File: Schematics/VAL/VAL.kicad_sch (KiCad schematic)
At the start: 2 parts

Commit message: Fox NOVRAM address bus
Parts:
- U101, U102: value (none) -> ~
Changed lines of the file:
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@@
   (wire (pts (xy 566.42 241.3) (xy 566.42 243.84) ) (stroke (width 0) (type default) ) )
   (wire (pts (xy 566.42 259.08) (xy 566.42 261.62) ) (stroke (width 0) (type default) ) )
-  (symbol (lib_id "r1000:PU") (at 566.42 241.3 0) (unit 1) (in_bom yes) (on_board yes) (property "Reference" "#PWR0102" (id 0) (at 566.42 241.3 0) (effects (font (size 1.27 1.27) ) hide ) ) (property "Value" "" (id 1) (at 566.42 241.3 0) (effects (font (size 1.27 1.27) ) hide ) ) (property "Footprint" "" (id 2) (at 566.42 241.3 0) (effects (font (size 1.27 1.27) ) hide ) ) (property "Datasheet" "" (id 3) (at 566.42 241.3 0) (effects (font (size 1.27 1.27) ) hide ) ) (pin "1" ) )
-  (symbol (lib_id "r1000:Pull_Down") (at 566.42 259.08 0) (unit 1) (in_bom yes) (on_board yes) (property "Reference" "U102" (id 0) (at 566.42 259.08 0) (effects (font (size 1.27 1.27) ) ) ) (property "Value" "" (id 1) (at 566.42 255.27 0) (effects (font (size 2.54 2.54) ) ) ) (property "Footprint" "" (id 2) (at 566.42 259.08 0) (effects (font (size 1.27 1.27) ) hide ) ) (property "Datasheet" "" (id 3) (at 566.42 259.08 0) (effects (font (size 1.27 1.27) ) hide ) ) (pin "1" ) )
-  (symbol (lib_id "r1000:Pull_Up") (at 566.42 243.84 0) (unit 1) (in_bom yes) (on_board yes) (property "Reference" "U101" (id 0) (at 566.42 243.84 0) (effects (font (size 1.27 1.27) ) ) ) (property "Value" "" (id 1) (at 566.42 247.65 0) (effects (font (size 2.54 2.54) ) ) ) (property "Footprint" "" (id 2) (at 566.42 243.84 0) (effects (font (size 1.27 1.27) ) hide ) ) (property "Datasheet" "" (id 3) (at 566.42 243.84 0) (effects (font (size 1.27 1.27) ) hide ) ) (pin "1" ) )
-  (symbol (lib_id "r1000:PD") (at 566.42 261.62 0) (unit 1) (in_bom no) (on_board yes) (property "Reference" "#PWR0101" (id 0) (at 566.42 261.62 0) (effects (font (size 1.27 1.27) ) hide ) ) (property "Value" "" (id 1) (at 566.42 261.62 0) (effects (font (size 1.27 1.27) ) hide ) ) (property "Footprint" "" (id 2) (at 566.42 261.62 0) (effects (font (size 1.27 1.27) ) hide ) ) (property "Datasheet" "" (id 3) (at 566.42 261.62 0) (effects (font (size 1.27 1.27) ) hide ) ) (pin "1" ) )
+  (symbol (lib_id "r1000:PU") (at 566.42 241.3 0) (unit 1) (in_bom yes) (on_board yes) (property "Reference" "#PWR0102" (id 0) (at 566.42 241.3 0) (effects (font (size 1.27 1.27) ) hide ) ) (property "Value" "~" (id 1) (at 566.42 241.3 0) (effects (font (size 1.27 1.27) ) hide ) ) (property "Footprint" "" (id 2) (at 566.42 241.3 0) (effects (font (size 1.27 1.27) ) hide ) ) (property "Datasheet" "" (id 3) (at 566.42 241.3 0) (effects (font (size 1.27 1.27) ) hide ) ) (pin "1" ) )
+  (symbol (lib_id "r1000:Pull_Down") (at 566.42 259.08 0) (unit 1) (in_bom yes) (on_board yes) (property "Reference" "U102" (id 0) (at 566.42 259.08 0) (effects (font (size 1.27 1.27) ) ) ) (property "Value" "~" (id 1) (at 566.42 255.27 0) (effects (font (size 2.54 2.54) ) ) ) (property "Footprint" "" (id 2) (at 566.42 259.08 0) (effects (font (size 1.27 1.27) ) hide ) ) (property "Datasheet" "" (id 3) (at 566.42 259.08 0) (effects (font (size 1.27 1.27) ) hide ) ) (pin "1" ) )
+  (symbol (lib_id "r1000:Pull_Up") (at 566.42 243.84 0) (unit 1) (in_bom yes) (on_board yes) (property "Reference" "U101" (id 0) (at 566.42 243.84 0) (effects (font (size 1.27 1.27) ) ) ) (property "Value" "~" (id 1) (at 566.42 247.65 0) (effects (font (size 2.54 2.54) ) ) ) (property "Footprint" "" (id 2) (at 566.42 243.84 0) (effects (font (size 1.27 1.27) ) hide ) ) (property "Datasheet" "" (id 3) (at 566.42 243.84 0) (effects (font (size 1.27 1.27) ) hide ) ) (pin "1" ) )
+  (symbol (lib_id "r1000:PD") (at 566.42 261.62 0) (unit 1) (in_bom no) (on_board yes) (property "Reference" "#PWR0101" (id 0) (at 566.42 261.62 0) (effects (font (size 1.27 1.27) ) hide ) ) (property "Value" "~" (id 1) (at 566.42 261.62 0) (effects (font (size 1.27 1.27) ) hide ) ) (property "Footprint" "" (id 2) (at 566.42 261.62 0) (effects (font (size 1.27 1.27) ) hide ) ) (property "Datasheet" "" (id 3) (at 566.42 261.62 0) (effects (font (size 1.27 1.27) ) hide ) ) (pin "1" ) )
   (text "Board: VAL Branch: megacomp2" (at 7.62 370.84 0) (effects (font (size 7.62 7.62) (thickness 1.27) bold ) (justify left bottom) ) )
   (sheet_instances

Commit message: Megacom WCS + parity
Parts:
- U101, U102: value ~ -> (none)
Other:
- note added: "WRITABLE CONTROL STORE - WCS BITS 32 TO 38 AND PARITY <6>"
- note removed: "WRITABLE CONTROL STORE - WCS BITS 32 TO 38 AND PARITY"
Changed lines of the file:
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@@
   (wire (pts (xy 566.42 241.3) (xy 566.42 243.84) ) (stroke (width 0) (type default) ) )
   (wire (pts (xy 566.42 259.08) (xy 566.42 261.62) ) (stroke (width 0) (type default) ) )
-  (symbol (lib_id "r1000:PU") (at 566.42 241.3 0) (unit 1) (in_bom yes) (on_board yes) (property "Reference" "#PWR0102" (id 0) (at 566.42 241.3 0) (effects (font (size 1.27 1.27) ) hide ) ) (property "Value" "~" (id 1) (at 566.42 241.3 0) (effects (font (size 1.27 1.27) ) hide ) ) (property "Footprint" "" (id 2) (at 566.42 241.3 0) (effects (font (size 1.27 1.27) ) hide ) ) (property "Datasheet" "" (id 3) (at 566.42 241.3 0) (effects (font (size 1.27 1.27) ) hide ) ) (pin "1" ) )
-  (symbol (lib_id "r1000:Pull_Down") (at 566.42 259.08 0) (unit 1) (in_bom yes) (on_board yes) (property "Reference" "U102" (id 0) (at 566.42 259.08 0) (effects (font (size 1.27 1.27) ) ) ) (property "Value" "~" (id 1) (at 566.42 255.27 0) (effects (font (size 2.54 2.54) ) ) ) (property "Footprint" "" (id 2) (at 566.42 259.08 0) (effects (font (size 1.27 1.27) ) hide ) ) (property "Datasheet" "" (id 3) (at 566.42 259.08 0) (effects (font (size 1.27 1.27) ) hide ) ) (pin "1" ) )
-  (symbol (lib_id "r1000:Pull_Up") (at 566.42 243.84 0) (unit 1) (in_bom yes) (on_board yes) (property "Reference" "U101" (id 0) (at 566.42 243.84 0) (effects (font (size 1.27 1.27) ) ) ) (property "Value" "~" (id 1) (at 566.42 247.65 0) (effects (font (size 2.54 2.54) ) ) ) (property "Footprint" "" (id 2) (at 566.42 243.84 0) (effects (font (size 1.27 1.27) ) hide ) ) (property "Datasheet" "" (id 3) (at 566.42 243.84 0) (effects (font (size 1.27 1.27) ) hide ) ) (pin "1" ) )
-  (symbol (lib_id "r1000:PD") (at 566.42 261.62 0) (unit 1) (in_bom no) (on_board yes) (property "Reference" "#PWR0101" (id 0) (at 566.42 261.62 0) (effects (font (size 1.27 1.27) ) hide ) ) (property "Value" "~" (id 1) (at 566.42 261.62 0) (effects (font (size 1.27 1.27) ) hide ) ) (property "Footprint" "" (id 2) (at 566.42 261.62 0) (effects (font (size 1.27 1.27) ) hide ) ) (property "Datasheet" "" (id 3) (at 566.42 261.62 0) (effects (font (size 1.27 1.27) ) hide ) ) (pin "1" ) )
+  (symbol (lib_id "r1000:PU") (at 566.42 241.3 0) (unit 1) (in_bom yes) (on_board yes) (property "Reference" "#PWR0102" (id 0) (at 566.42 241.3 0) (effects (font (size 1.27 1.27) ) hide ) ) (property "Value" "" (id 1) (at 566.42 241.3 0) (effects (font (size 1.27 1.27) ) hide ) ) (property "Footprint" "" (id 2) (at 566.42 241.3 0) (effects (font (size 1.27 1.27) ) hide ) ) (property "Datasheet" "" (id 3) (at 566.42 241.3 0) (effects (font (size 1.27 1.27) ) hide ) ) (pin "1" ) )
+  (symbol (lib_id "r1000:Pull_Down") (at 566.42 259.08 0) (unit 1) (in_bom yes) (on_board yes) (property "Reference" "U102" (id 0) (at 566.42 259.08 0) (effects (font (size 1.27 1.27) ) ) ) (property "Value" "" (id 1) (at 566.42 255.27 0) (effects (font (size 2.54 2.54) ) ) ) (property "Footprint" "" (id 2) (at 566.42 259.08 0) (effects (font (size 1.27 1.27) ) hide ) ) (property "Datasheet" "" (id 3) (at 566.42 259.08 0) (effects (font (size 1.27 1.27) ) hide ) ) (pin "1" ) )
+  (symbol (lib_id "r1000:Pull_Up") (at 566.42 243.84 0) (unit 1) (in_bom yes) (on_board yes) (property "Reference" "U101" (id 0) (at 566.42 243.84 0) (effects (font (size 1.27 1.27) ) ) ) (property "Value" "" (id 1) (at 566.42 247.65 0) (effects (font (size 2.54 2.54) ) ) ) (property "Footprint" "" (id 2) (at 566.42 243.84 0) (effects (font (size 1.27 1.27) ) hide ) ) (property "Datasheet" "" (id 3) (at 566.42 243.84 0) (effects (font (size 1.27 1.27) ) hide ) ) (pin "1" ) )
+  (symbol (lib_id "r1000:PD") (at 566.42 261.62 0) (unit 1) (in_bom no) (on_board yes) (property "Reference" "#PWR0101" (id 0) (at 566.42 261.62 0) (effects (font (size 1.27 1.27) ) hide ) ) (property "Value" "" (id 1) (at 566.42 261.62 0) (effects (font (size 1.27 1.27) ) hide ) ) (property "Footprint" "" (id 2) (at 566.42 261.62 0) (effects (font (size 1.27 1.27) ) hide ) ) (property "Datasheet" "" (id 3) (at 566.42 261.62 0) (effects (font (size 1.27 1.27) ) hide ) ) (pin "1" ) )
   (text "Board: VAL Branch: megacomp2" (at 7.62 370.84 0) (effects (font (size 7.62 7.62) (thickness 1.27) bold ) (justify left bottom) ) )
   (sheet_instances
@@
   (sheet (at 266.70 88.90) (size 20.32 5.08) (property "Sheet name" "Page 55" (id 0) (at 289.56 93.98 0) (effects (font (size 2.54 2.54) ) (justify left bottom) ) ) (property "Sheet file" "pg_55.kicad_sch" (id 1) (at 289.56 91.44 0) (effects (justify left bottom) hide ) ) (fill (color 192 192 192 1.0) ) )
   (text "WRITABLE CONTROL STORE - WCS BITS 16 to 31 <6>" (at 307.34 93.98 0) (effects (font (size 2.54 2.54) ) (justify left bottom) ) )
-  (sheet (at 266.70 96.52) (size 20.32 5.08) (property "Sheet name" "Page 56" (id 0) (at 289.56 101.60 0) (effects (font (size 2.54 2.54) ) (justify left bottom) ) ) (property "Sheet file" "pg_56.kicad_sch" (id 1) (at 289.56 99.06 0) (effects (justify left bottom) hide ) ) )
-  (text "WRITABLE CONTROL STORE - WCS BITS 32 TO 38 AND PARITY" (at 307.34 101.60 0) (effects (font (size 2.54 2.54) ) (justify left bottom) ) )
+  (sheet (at 266.70 96.52) (size 20.32 5.08) (property "Sheet name" "Page 56" (id 0) (at 289.56 101.60 0) (effects (font (size 2.54 2.54) ) (justify left bottom) ) ) (property "Sheet file" "pg_56.kicad_sch" (id 1) (at 289.56 99.06 0) (effects (justify left bottom) hide ) ) (fill (color 192 192 192 1.0) ) )
+  (text "WRITABLE CONTROL STORE - WCS BITS 32 TO 38 AND PARITY <6>" (at 307.34 101.60 0) (effects (font (size 2.54 2.54) ) (justify left bottom) ) )
   (sheet (at 266.70 104.14) (size 20.32 5.08) (property "Sheet name" "Page 57" (id 0) (at 289.56 109.22 0) (effects (font (size 2.54 2.54) ) (justify left bottom) ) ) (property "Sheet file" "pg_57.kicad_sch" (id 1) (at 289.56 106.68 0) (effects (justify left bottom) hide ) ) )
   (text "WRITABLE CONTROL STORE - MICRO INSTRUCTION REGISTER" (at 307.34 109.22 0) (effects (font (size 2.54 2.54) ) (justify left bottom) ) )

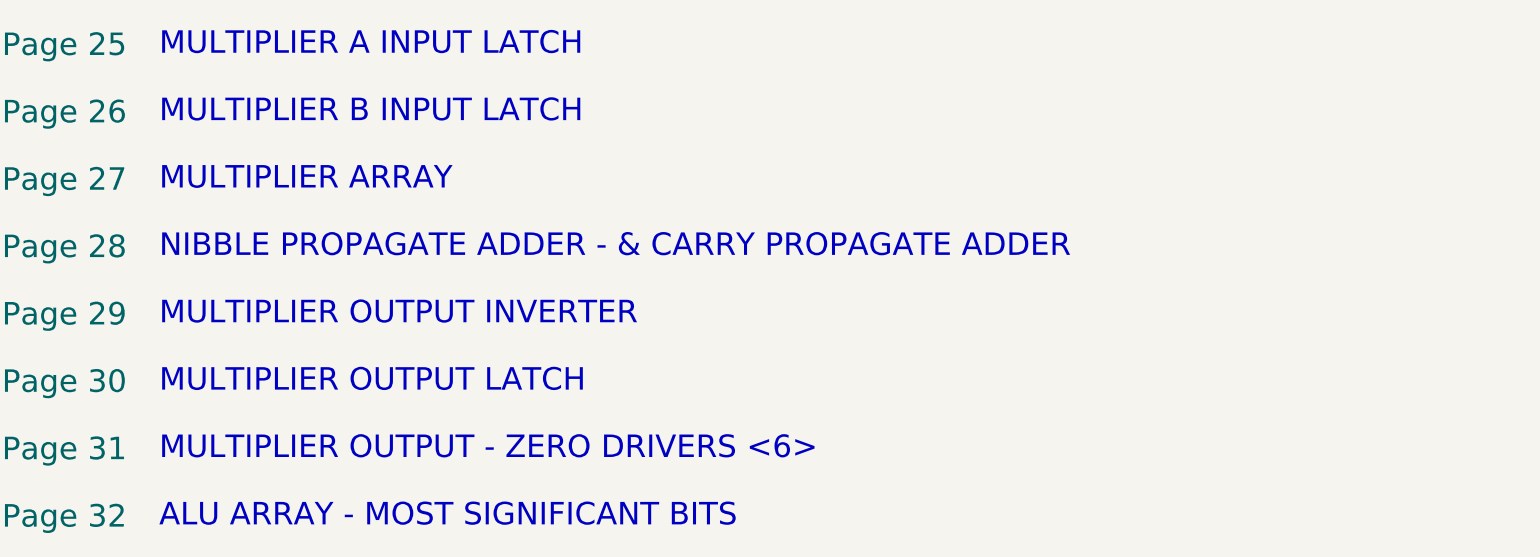
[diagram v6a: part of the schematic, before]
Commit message: Megacomp/polish work on VAL (incl. megacomp multiplier)
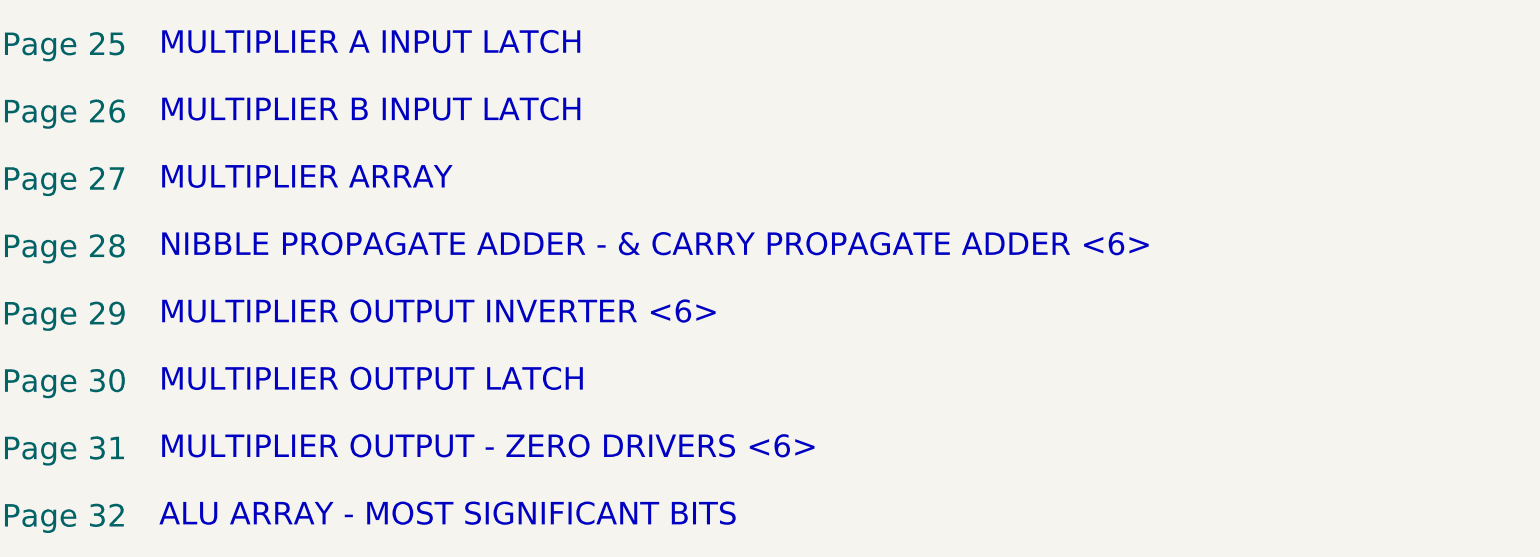
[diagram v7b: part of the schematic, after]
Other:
- note added: "MULTIPLIER OUTPUT INVERTER <6>"
- note added: "NIBBLE PROPAGATE ADDER - & CARRY PROPAGATE ADDER <6>"
- note removed: "MULTIPLIER OUTPUT INVERTER"
- note removed: "NIBBLE PROPAGATE ADDER - & CARRY PROPAGATE ADDER"
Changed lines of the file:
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@@
   (sheet (at 12.70 218.44) (size 20.32 5.08) (property "Sheet name" "Page 27" (id 0) (at 35.56 223.52 0) (effects (font (size 2.54 2.54) ) (justify left bottom) ) ) (property "Sheet file" "pg_27.kicad_sch" (id 1) (at 35.56 220.98 0) (effects (justify left bottom) hide ) ) )
   (text "MULTIPLIER ARRAY" (at 53.34 223.52 0) (effects (font (size 2.54 2.54) ) (justify left bottom) ) )
-  (sheet (at 12.70 226.06) (size 20.32 5.08) (property "Sheet name" "Page 28" (id 0) (at 35.56 231.14 0) (effects (font (size 2.54 2.54) ) (justify left bottom) ) ) (property "Sheet file" "pg_28.kicad_sch" (id 1) (at 35.56 228.60 0) (effects (justify left bottom) hide ) ) )
-  (text "NIBBLE PROPAGATE ADDER - & CARRY PROPAGATE ADDER" (at 53.34 231.14 0) (effects (font (size 2.54 2.54) ) (justify left bottom) ) )
-  (sheet (at 12.70 233.68) (size 20.32 5.08) (property "Sheet name" "Page 29" (id 0) (at 35.56 238.76 0) (effects (font (size 2.54 2.54) ) (justify left bottom) ) ) (property "Sheet file" "pg_29.kicad_sch" (id 1) (at 35.56 236.22 0) (effects (justify left bottom) hide ) ) )
-  (text "MULTIPLIER OUTPUT INVERTER" (at 53.34 238.76 0) (effects (font (size 2.54 2.54) ) (justify left bottom) ) )
+  (sheet (at 12.70 226.06) (size 20.32 5.08) (property "Sheet name" "Page 28" (id 0) (at 35.56 231.14 0) (effects (font (size 2.54 2.54) ) (justify left bottom) ) ) (property "Sheet file" "pg_28.kicad_sch" (id 1) (at 35.56 228.60 0) (effects (justify left bottom) hide ) ) (fill (color 192 192 192 1.0) ) )
+  (text "NIBBLE PROPAGATE ADDER - & CARRY PROPAGATE ADDER <6>" (at 53.34 231.14 0) (effects (font (size 2.54 2.54) ) (justify left bottom) ) )
+  (sheet (at 12.70 233.68) (size 20.32 5.08) (property "Sheet name" "Page 29" (id 0) (at 35.56 238.76 0) (effects (font (size 2.54 2.54) ) (justify left bottom) ) ) (property "Sheet file" "pg_29.kicad_sch" (id 1) (at 35.56 236.22 0) (effects (justify left bottom) hide ) ) (fill (color 192 192 192 1.0) ) )
+  (text "MULTIPLIER OUTPUT INVERTER <6>" (at 53.34 238.76 0) (effects (font (size 2.54 2.54) ) (justify left bottom) ) )
   (sheet (at 12.70 241.30) (size 20.32 5.08) (property "Sheet name" "Page 30" (id 0) (at 35.56 246.38 0) (effects (font (size 2.54 2.54) ) (justify left bottom) ) ) (property "Sheet file" "pg_30.kicad_sch" (id 1) (at 35.56 243.84 0) (effects (justify left bottom) hide ) ) )
   (text "MULTIPLIER OUTPUT LATCH" (at 53.34 246.38 0) (effects (font (size 2.54 2.54) ) (justify left bottom) ) )
